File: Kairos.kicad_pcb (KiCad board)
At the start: 2 copper layers, 285 x 94.6 mm, 133 parts, among them Q1 NSS40301MZ4T1G, SW1 SW_RST1, U1 ATMEGA32U2-AU, Y1 Crystal_GND24

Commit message: Fix wrong size footprints (Hopefully all of them)
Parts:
- K_TAB1, K_\1: footprint MX_Alps_Hybrid:MX-1U -> MX_Alps_Hybrid:MX-1.5U
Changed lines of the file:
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@@
     (pad "" np_thru_hole circle (at 57.15 -8.255) (size 3.9878 3.9878) (drill 3.9878) (layers *.Cu *.Mask))
-  )
-  (module MX_Alps_Hybrid:MX-1U (layer F.Cu)
-    (at 19.05 50.00625)
-    (fp_text reference K_TAB1 (at 0 3.175) (layer F.SilkS)
-      (effects (font (size 1 1) (thickness 0.15)))
-    )
-    (fp_text value MX-1.5U (at 0 -7.9375) (layer Dwgs.User)
-      (effects (font (size 1 1) (thickness 0.15)))
-    )
-    (fp_line (start 5 -7) (end 7 -7) (layer Dwgs.User) (width 0.15))
-    (fp_line (start 7 -7) (end 7 -5) (layer Dwgs.User) (width 0.15))
-    (fp_line (start 5 7) (end 7 7) (layer Dwgs.User) (width 0.15))
-    (fp_line (start 7 7) (end 7 5) (layer Dwgs.User) (width 0.15))
-    (fp_line (start -7 5) (end -7 7) (layer Dwgs.User) (width 0.15))
-    (fp_line (start -7 7) (end -5 7) (layer Dwgs.User) (width 0.15))
-    (fp_line (start -5 -7) (end -7 -7) (layer Dwgs.User) (width 0.15))
-    (fp_line (start -7 -7) (end -7 -5) (layer Dwgs.User) (width 0.15))
-    (fp_line (start -9.525 -9.525) (end 9.525 -9.525) (layer Dwgs.User) (width 0.15))
-    (fp_line (start 9.525 -9.525) (end 9.525 9.525) (layer Dwgs.User) (width 0.15))
-    (fp_line (start 9.525 9.525) (end -9.525 9.525) (layer Dwgs.User) (width 0.15))
-    (fp_line (start -9.525 9.525) (end -9.525 -9.525) (layer Dwgs.User) (width 0.15))
-    (pad 2 thru_hole oval (at 2.5 -4.5 86.0548) (size 2.831378 2.25) (drill 1.47 (offset 0.290689 0)) (layers *.Cu *.Mask)
-      (net 163 "Net-(DTAB1-Pad2)"))
-    (pad 2 thru_hole circle (at 2.54 -5.08) (size 2.25 2.25) (drill 1.47) (layers *.Cu *.Mask)
-      (net 163 "Net-(DTAB1-Pad2)"))
-    (pad 1 thru_hole oval (at -3.81 -2.54 48.09963212) (size 4.211556 2.25) (drill 1.47 (offset 0.980778 0)) (layers *.Cu *.Mask)
-      (net 109 COL1))
-    (pad "" np_thru_hole circle (at 0 0) (size 3.9878 3.9878) (drill 3.9878) (layers *.Cu *.Mask))
-    (pad 1 thru_hole circle (at -2.5 -4) (size 2.25 2.25) (drill 1.47) (layers *.Cu *.Mask)
-      (net 109 COL1))
-    (pad 3 thru_hole circle (at -1.27 5.08) (size 1.905 1.905) (drill 1.04) (layers *.Cu *.Mask)
-      (net 53 "Net-(K_TAB1-Pad3)"))
-    (pad 4 thru_hole rect (at 1.27 5.08) (size 1.905 1.905) (drill 1.04) (layers *.Cu *.Mask)
-      (net 2 LEDGND))
-    (pad "" np_thru_hole circle (at -5.08 0 48.0996) (size 1.7018 1.7018) (drill 1.7018) (layers *.Cu *.Mask))
-    (pad "" np_thru_hole circle (at 5.08 0 48.0996) (size 1.7018 1.7018) (drill 1.7018) (layers *.Cu *.Mask))
-  )
-  (module MX_Alps_Hybrid:MX-1U (layer F.Cu)
-    (at 276.225 50.00625)
-    (fp_text reference K_\1 (at 0 3.175) (layer F.SilkS)
-      (effects (font (size 1 1) (thickness 0.15)))
-    )
-    (fp_text value MX-1.5U (at 0 -7.9375) (layer Dwgs.User)
-      (effects (font (size 1 1) (thickness 0.15)))
-    )
-    (fp_line (start 5 -7) (end 7 -7) (layer Dwgs.User) (width 0.15))
-    (fp_line (start 7 -7) (end 7 -5) (layer Dwgs.User) (width 0.15))
-    (fp_line (start 5 7) (end 7 7) (layer Dwgs.User) (width 0.15))
-    (fp_line (start 7 7) (end 7 5) (layer Dwgs.User) (width 0.15))
-    (fp_line (start -7 5) (end -7 7) (layer Dwgs.User) (width 0.15))
-    (fp_line (start -7 7) (end -5 7) (layer Dwgs.User) (width 0.15))
-    (fp_line (start -5 -7) (end -7 -7) (layer Dwgs.User) (width 0.15))
-    (fp_line (start -7 -7) (end -7 -5) (layer Dwgs.User) (width 0.15))
-    (fp_line (start -9.525 -9.525) (end 9.525 -9.525) (layer Dwgs.User) (width 0.15))
-    (fp_line (start 9.525 -9.525) (end 9.525 9.525) (layer Dwgs.User) (width 0.15))
-    (fp_line (start 9.525 9.525) (end -9.525 9.525) (layer Dwgs.User) (width 0.15))
-    (fp_line (start -9.525 9.525) (end -9.525 -9.525) (layer Dwgs.User) (width 0.15))
-    (pad 2 thru_hole oval (at 2.5 -4.5 86.0548) (size 2.831378 2.25) (drill 1.47 (offset 0.290689 0)) (layers *.Cu *.Mask)
-      (net 171 "Net-(D\\1-Pad2)"))
-    (pad 2 thru_hole circle (at 2.54 -5.08) (size 2.25 2.25) (drill 1.47) (layers *.Cu *.Mask)
-      (net 171 "Net-(D\\1-Pad2)"))
-    (pad 1 thru_hole oval (at -3.81 -2.54 48.09963212) (size 4.211556 2.25) (drill 1.47 (offset 0.980778 0)) (layers *.Cu *.Mask)
-      (net 130 COL7))
-    (pad "" np_thru_hole circle (at 0 0) (size 3.9878 3.9878) (drill 3.9878) (layers *.Cu *.Mask))
-    (pad 1 thru_hole circle (at -2.5 -4) (size 2.25 2.25) (drill 1.47) (layers *.Cu *.Mask)
-      (net 130 COL7))
-    (pad 3 thru_hole circle (at -1.27 5.08) (size 1.905 1.905) (drill 1.04) (layers *.Cu *.Mask)
-      (net 61 "Net-(K_\\1-Pad3)"))
-    (pad 4 thru_hole rect (at 1.27 5.08) (size 1.905 1.905) (drill 1.04) (layers *.Cu *.Mask)
-      (net 2 LEDGND))
-    (pad "" np_thru_hole circle (at -5.08 0 48.0996) (size 1.7018 1.7018) (drill 1.7018) (layers *.Cu *.Mask))
-    (pad "" np_thru_hole circle (at 5.08 0 48.0996) (size 1.7018 1.7018) (drill 1.7018) (layers *.Cu *.Mask))
   )
   (module MX_Alps_Hybrid:MX-6U-7UOverlay (layer F.Cu)
@@
     (pad "" np_thru_hole circle (at 8.255 -11.90625) (size 3.9878 3.9878) (drill 3.9878) (layers *.Cu *.Mask))
   )
+  (module MX_Alps_Hybrid:MX-1.5U (layer F.Cu)
+    (at 19.05 50.00625)
+    (fp_text reference K_TAB1 (at 0 3.175) (layer F.SilkS)
+      (effects (font (size 1 1) (thickness 0.15)))
+    )
+    (fp_text value MX-1.5U (at 0 -7.9375) (layer Dwgs.User)
+      (effects (font (size 1 1) (thickness 0.15)))
+    )
+    (fp_line (start 5 -7) (end 7 -7) (layer Dwgs.User) (width 0.15))
+    (fp_line (start 7 -7) (end 7 -5) (layer Dwgs.User) (width 0.15))
+    (fp_line (start 5 7) (end 7 7) (layer Dwgs.User) (width 0.15))
+    (fp_line (start 7 7) (end 7 5) (layer Dwgs.User) (width 0.15))
+    (fp_line (start -7 5) (end -7 7) (layer Dwgs.User) (width 0.15))
+    (fp_line (start -7 7) (end -5 7) (layer Dwgs.User) (width 0.15))
+    (fp_line (start -5 -7) (end -7 -7) (layer Dwgs.User) (width 0.15))
+    (fp_line (start -7 -7) (end -7 -5) (layer Dwgs.User) (width 0.15))
+    (fp_line (start -14.2875 -9.525) (end 14.2875 -9.525) (layer Dwgs.User) (width 0.15))
+    (fp_line (start 14.2875 -9.525) (end 14.2875 9.525) (layer Dwgs.User) (width 0.15))
+    (fp_line (start -14.2875 9.525) (end 14.2875 9.525) (layer Dwgs.User) (width 0.15))
+    (fp_line (start -14.2875 9.525) (end -14.2875 -9.525) (layer Dwgs.User) (width 0.15))
+    (pad 2 thru_hole oval (at 2.5 -4.5 86.0548) (size 2.831378 2.25) (drill 1.47 (offset 0.290689 0)) (layers *.Cu *.Mask)
+      (net 163 "Net-(DTAB1-Pad2)"))
+    (pad 2 thru_hole circle (at 2.54 -5.08) (size 2.25 2.25) (drill 1.47) (layers *.Cu *.Mask)
+      (net 163 "Net-(DTAB1-Pad2)"))
+    (pad 1 thru_hole oval (at -3.81 -2.54 48.09963212) (size 4.211556 2.25) (drill 1.47 (offset 0.980778 0)) (layers *.Cu *.Mask)
+      (net 109 COL1))
+    (pad "" np_thru_hole circle (at 0 0) (size 3.9878 3.9878) (drill 3.9878) (layers *.Cu *.Mask))
+    (pad 1 thru_hole circle (at -2.5 -4) (size 2.25 2.25) (drill 1.47) (layers *.Cu *.Mask)
+      (net 109 COL1))
+    (pad 3 thru_hole circle (at -1.27 5.08) (size 1.905 1.905) (drill 1.04) (layers *.Cu *.Mask)
+      (net 53 "Net-(K_TAB1-Pad3)"))
+    (pad 4 thru_hole rect (at 1.27 5.08) (size 1.905 1.905) (drill 1.04) (layers *.Cu *.Mask)
+      (net 2 LEDGND))
+    (pad "" np_thru_hole circle (at -5.08 0 48.0996) (size 1.7018 1.7018) (drill 1.7018) (layers *.Cu *.Mask))
+    (pad "" np_thru_hole circle (at 5.08 0 48.0996) (size 1.7018 1.7018) (drill 1.7018) (layers *.Cu *.Mask))
+  )
+  (module MX_Alps_Hybrid:MX-1.5U (layer F.Cu)
+    (at 276.225 50.00625)
+    (fp_text reference K_\1 (at 0 3.175) (layer F.SilkS)
+      (effects (font (size 1 1) (thickness 0.15)))
+    )
+    (fp_text value MX-1.5U (at 0 -7.9375) (layer Dwgs.User)
+      (effects (font (size 1 1) (thickness 0.15)))
+    )
+    (fp_line (start 5 -7) (end 7 -7) (layer Dwgs.User) (width 0.15))
+    (fp_line (start 7 -7) (end 7 -5) (layer Dwgs.User) (width 0.15))
+    (fp_line (start 5 7) (end 7 7) (layer Dwgs.User) (width 0.15))
+    (fp_line (start 7 7) (end 7 5) (layer Dwgs.User) (width 0.15))
+    (fp_line (start -7 5) (end -7 7) (layer Dwgs.User) (width 0.15))
+    (fp_line (start -7 7) (end -5 7) (layer Dwgs.User) (width 0.15))
+    (fp_line (start -5 -7) (end -7 -7) (layer Dwgs.User) (width 0.15))
+    (fp_line (start -7 -7) (end -7 -5) (layer Dwgs.User) (width 0.15))
+    (fp_line (start -14.2875 -9.525) (end 14.2875 -9.525) (layer Dwgs.User) (width 0.15))
+    (fp_line (start 14.2875 -9.525) (end 14.2875 9.525) (layer Dwgs.User) (width 0.15))
+    (fp_line (start -14.2875 9.525) (end 14.2875 9.525) (layer Dwgs.User) (width 0.15))
+    (fp_line (start -14.2875 9.525) (end -14.2875 -9.525) (layer Dwgs.User) (width 0.15))
+    (pad 2 thru_hole oval (at 2.5 -4.5 86.0548) (size 2.831378 2.25) (drill 1.47 (offset 0.290689 0)) (layers *.Cu *.Mask)
+      (net 171 "Net-(D\\1-Pad2)"))
+    (pad 2 thru_hole circle (at 2.54 -5.08) (size 2.25 2.25) (drill 1.47) (layers *.Cu *.Mask)
+      (net 171 "Net-(D\\1-Pad2)"))
+    (pad 1 thru_hole oval (at -3.81 -2.54 48.09963212) (size 4.211556 2.25) (drill 1.47 (offset 0.980778 0)) (layers *.Cu *.Mask)
+      (net 130 COL7))
+    (pad "" np_thru_hole circle (at 0 0) (size 3.9878 3.9878) (drill 3.9878) (layers *.Cu *.Mask))
+    (pad 1 thru_hole circle (at -2.5 -4) (size 2.25 2.25) (drill 1.47) (layers *.Cu *.Mask)
+      (net 130 COL7))
+    (pad 3 thru_hole circle (at -1.27 5.08) (size 1.905 1.905) (drill 1.04) (layers *.Cu *.Mask)
+      (net 61 "Net-(K_\\1-Pad3)"))
+    (pad 4 thru_hole rect (at 1.27 5.08) (size 1.905 1.905) (drill 1.04) (layers *.Cu *.Mask)
+      (net 2 LEDGND))
+    (pad "" np_thru_hole circle (at -5.08 0 48.0996) (size 1.7018 1.7018) (drill 1.7018) (layers *.Cu *.Mask))
+    (pad "" np_thru_hole circle (at 5.08 0 48.0996) (size 1.7018 1.7018) (drill 1.7018) (layers *.Cu *.Mask))
+  )
   (gr_text 107.15625 (at 237.33125 150.8125) (layer Dwgs.User)

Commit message: Fixed most led positions
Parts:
- K_LM2: footprint MX_Alps_Hybrid:MX-1.5U -> MX_Alps_Hybrid:MX-1.5U-FLIPPED
- K_LS1: footprint MX_Alps_Hybrid:MX-2.25U -> MX_Alps_Hybrid:MX-2.25U-FLIPPED
- K_LS5, K_RS3: footprint MX_Alps_Hybrid:MX-1.25U -> MX_Alps_Hybrid:MX-1.25U-FLIPPED
- K_RS6: footprint MX_Alps_Hybrid:MX-2.75U -> MX_Alps_Hybrid:MX-2.75U-FLIPPED
- K_RS8: footprint MX_Alps_Hybrid:MX-1.75U -> MX_Alps_Hybrid:MX-1.75U-FLIPPED

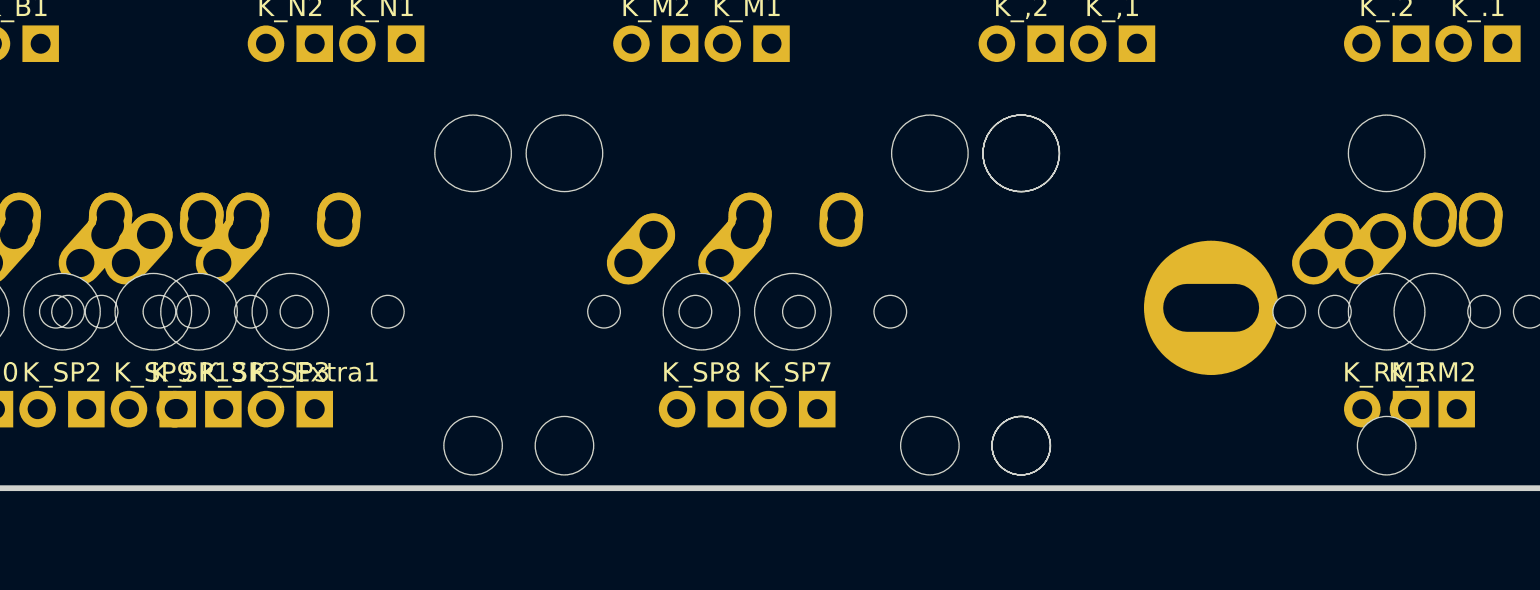
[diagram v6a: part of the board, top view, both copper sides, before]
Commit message: Add 7U Split Spacebar
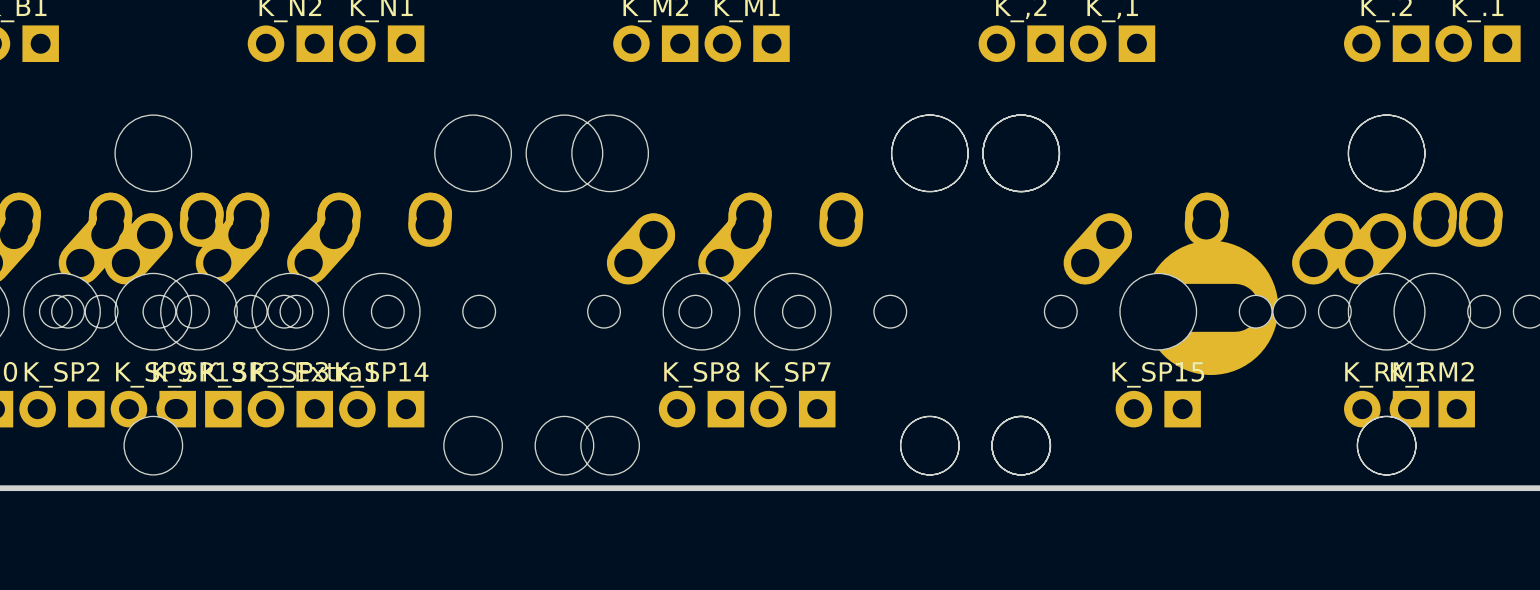
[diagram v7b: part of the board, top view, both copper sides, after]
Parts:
- added K_SP14: MX-2U, MX_Alps_Hybrid:MX-2U-ReversedStabilizers, F.Cu at (152.4, 107.2)
- added K_SP15: MX-2.25U, MX_Alps_Hybrid:MX-2.25U-ReversedStabilizer, F.Cu at (192.9, 107.2)

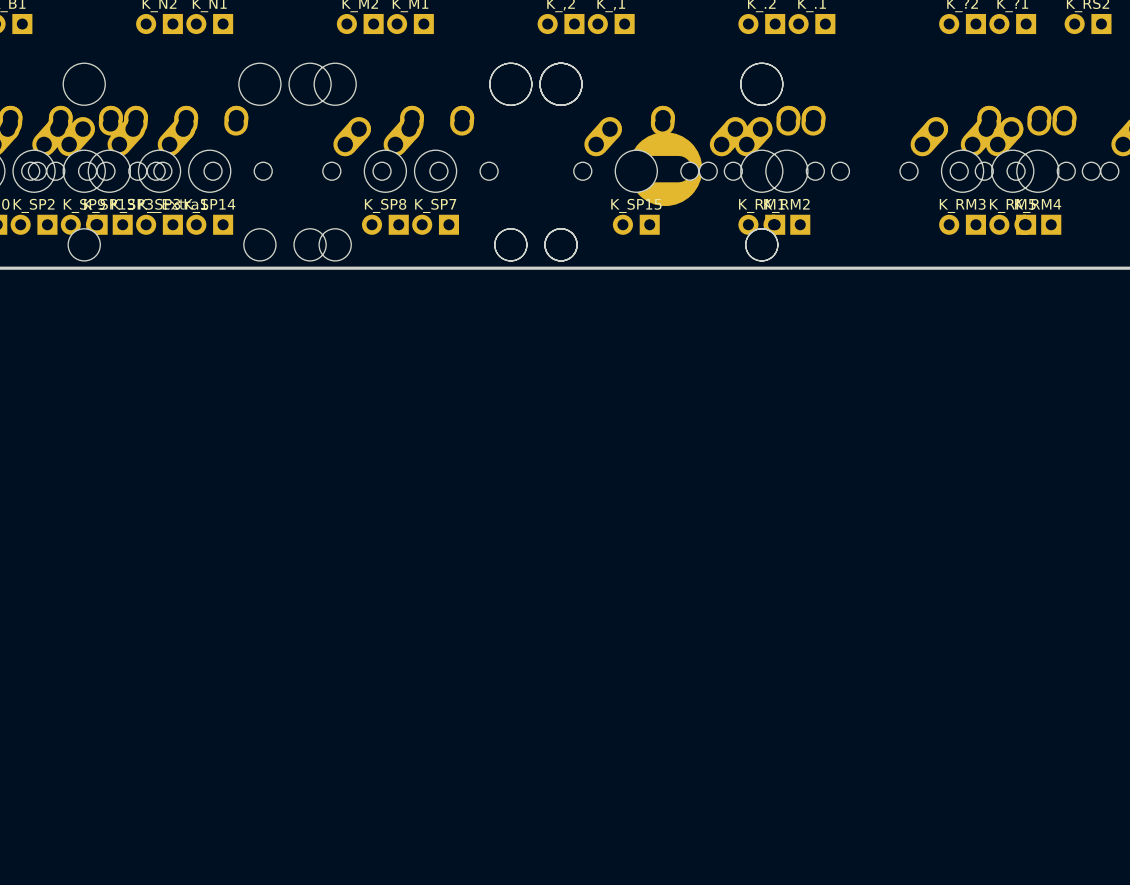
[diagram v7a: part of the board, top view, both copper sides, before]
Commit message: Reverse order in schematic, load changes
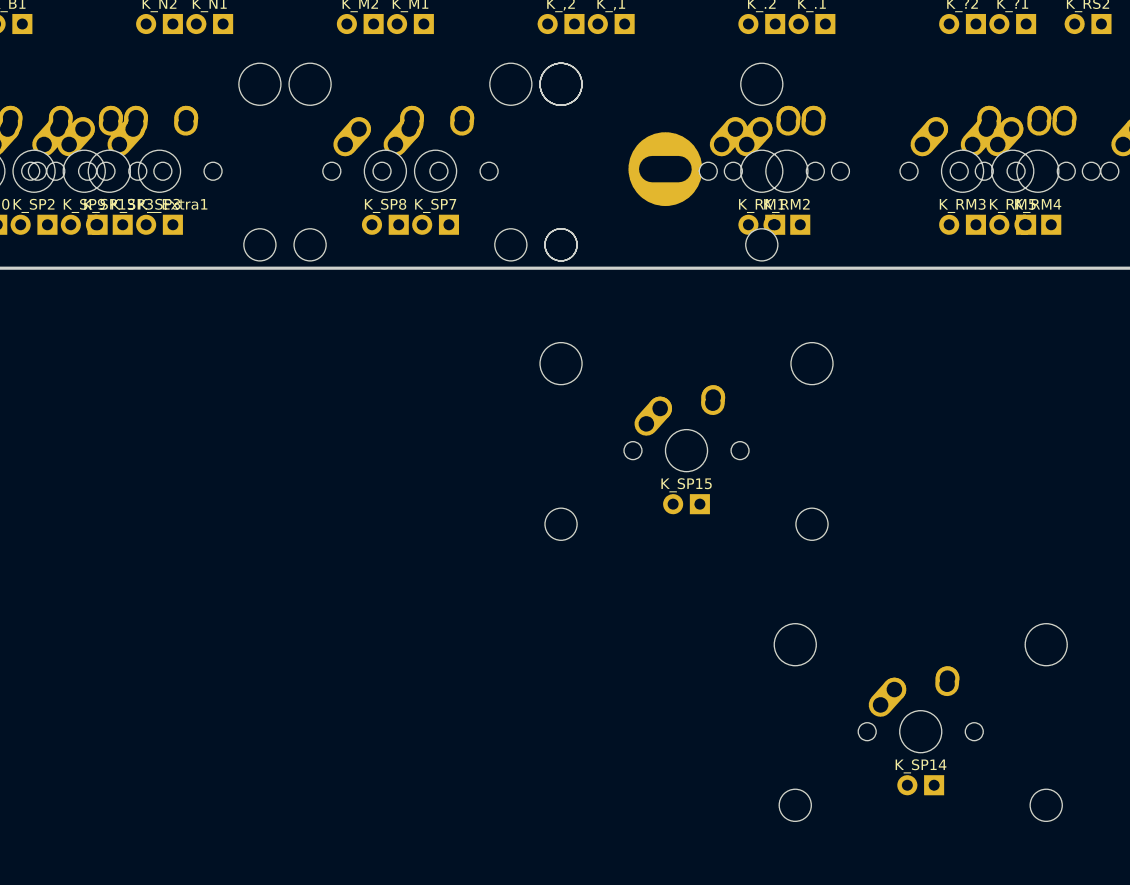
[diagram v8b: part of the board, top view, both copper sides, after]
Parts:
- K_SP14: value MX-2U -> MX-2.25U
- K_SP15: value MX-2.25U -> MX-2.75U
- moved K_SP14 85.9 mm to (219.9, 160.3)
- moved K_SP15 26.9 mm to (197.6, 133.7)
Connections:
- K_SP14 pad 2: COL4 -> COL3
- K_SP14 pad 3: Net-(K_SP10-Pad3) -> Net-(K_SP11-Pad3)
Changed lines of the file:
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@@
   (general
     (links 581)
-    (no_connects 306)
+    (no_connects 307)
     (area 0 0 0 0)
     (thickness 1.6)
@@
   )
   (module MX_Alps_Hybrid:MX-2U-ReversedStabilizers (layer F.Cu)
-    (at 152.4 107.15625)
+    (at 219.86875 160.3375)
     (fp_text reference K_SP14 (at 0 3.175) (layer F.SilkS)
       (effects (font (size 1 1) (thickness 0.15)))
     )
-    (fp_text value MX-2U (at 0 -7.9375) (layer Dwgs.User)
+    (fp_text value MX-2.25U (at 0 -7.9375) (layer Dwgs.User)
       (effects (font (size 1 1) (thickness 0.15)))
     )
@@
     (fp_line (start -19.05 9.525) (end -19.05 -9.525) (layer Dwgs.User) (width 0.15))
     (pad 2 thru_hole oval (at 2.5 -4.5 86.0548) (size 2.831378 2.25) (drill 1.47 (offset 0.290689 0)) (layers *.Cu *.Mask)
-      (net 74 COL4))
+      (net 75 COL3))
     (pad 2 thru_hole circle (at 2.54 -5.08) (size 2.25 2.25) (drill 1.47) (layers *.Cu *.Mask)
-      (net 74 COL4))
+      (net 75 COL3))
     (pad 1 thru_hole oval (at -3.81 -2.54 48.09963212) (size 4.211556 2.25) (drill 1.47 (offset 0.980778 0)) (layers *.Cu *.Mask)
       (net 35 ROW8))
@@
       (net 35 ROW8))
     (pad 3 thru_hole circle (at -1.27 5.08) (size 1.905 1.905) (drill 1.04) (layers *.Cu *.Mask)
-      (net 186 "Net-(K_SP10-Pad3)"))
+      (net 76 "Net-(K_SP11-Pad3)"))
     (pad 4 thru_hole rect (at 1.27 5.08) (size 1.905 1.905) (drill 1.04) (layers *.Cu *.Mask)
       (net 2 LEDGND))
@@
   )
   (module MX_Alps_Hybrid:MX-2.25U-ReversedStabilizer (layer F.Cu)
-    (at 192.88125 107.15625)
+    (at 197.64375 133.6675)
     (fp_text reference K_SP15 (at 0 3.175) (layer F.SilkS)
       (effects (font (size 1 1) (thickness 0.15)))
     )
-    (fp_text value MX-2.25U (at 0 -7.9375) (layer Dwgs.User)
+    (fp_text value MX-2.75U (at 0 -7.9375) (layer Dwgs.User)
       (effects (font (size 1 1) (thickness 0.15)))
     )
